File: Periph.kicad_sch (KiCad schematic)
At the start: 9 parts, among them U10 W25Q128JVSS, U8 ICM-42688-P

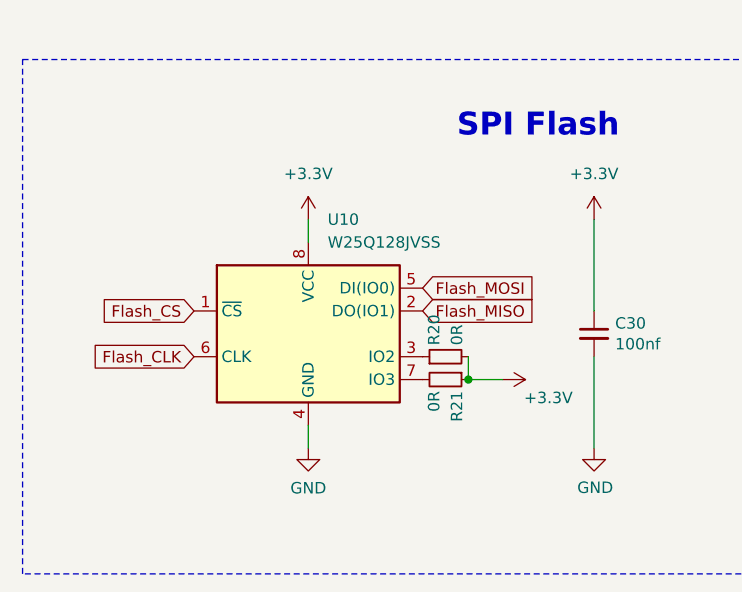
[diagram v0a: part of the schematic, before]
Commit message: update spi flash and ws2812b
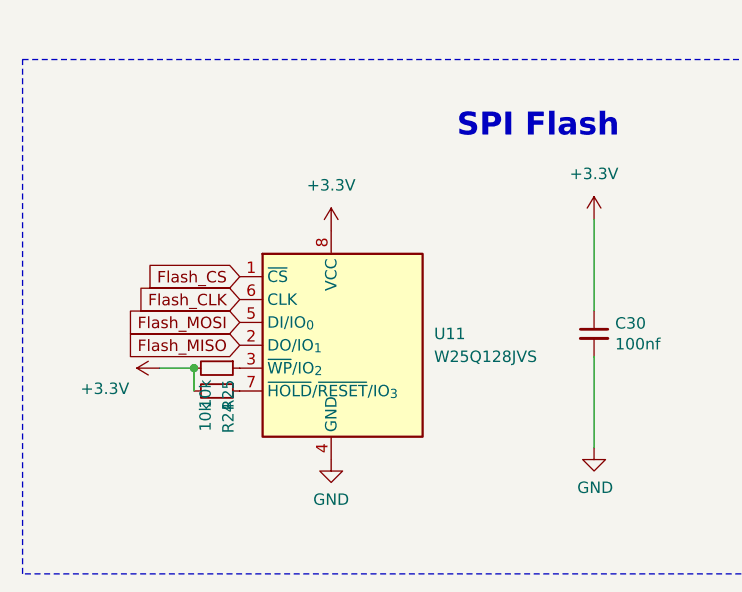
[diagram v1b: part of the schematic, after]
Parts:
- removed R20, R21: 0R, Resistor_SMD:R_0402_1005Metric, symbol Device:R_Small
- removed U10: W25Q128JVSS, Package_SO:SOIC-8_5.23x5.23mm_P1.27mm, symbol Memory_Flash:W25Q32JVSS
- added R24, R25: 10k, Resistor_SMD:R_0402_1005Metric, symbol Device:R_Small
- added U11: W25Q128JVS, Package_SO:SOIC-8_5.3x5.3mm_P1.27mm, symbol Memory_Flash:W25Q128JVS
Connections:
- net +3.3V: now also R24.2, R25.2, U11.8 (VCC)
- net Flash_CLK: now also U11.6 (CLK)
- net Flash_CS: now also U11.1 (~{CS})
- net Flash_MISO: now also U11.2 (DO/IO_{1})
- net Flash_MOSI: now also U11.5 (DI/IO_{0})
- net GND: now also U11.4 (GND)
- new net: R25.1, U11.3 (~{WP}/IO_{2})
- new net: R24.1, U11.7 (~{HOLD}/~{RESET}/IO_{3})

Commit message: update library
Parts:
- C24: renamed from C23; value 0.1u -> C_Small
- C25: renamed from C24; value 2u2 -> C_Small
- C26: renamed from C25; value 10n -> C_Small
- C27: renamed from C30; value 100nf -> C_Small
- R12: renamed from R19; value 10k -> R_Small
- R13: renamed from R25; value 10k -> R_Small
- R14: renamed from R24; value 10k -> R_Small
- U8: footprint mylib:PQFN50P300X250X97-14N -> ICM-42688-P:PQFN50P300X250X97-14N
- renumbered U11 to U9
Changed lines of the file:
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@@
 		(on_board yes)
 		(dnp no)
-		(property "Reference" "R25"
+		(property "Reference" "R13"
 			(at 67.31 151.13 0)
 			(effects
@@
 			)
 		)
-		(property "Value" "10k"
+		(property "Value" "R_Small"
 			(at 64.77 151.13 0)
 			(effects
@@
 			(project "MX_IMU"
 				(path "/8ed38441-7d4e-4e89-870f-07e11c6dce38/57f4b5bf-da86-4b65-9b05-7c9ef99c472c"
-					(reference "R25")
+					(reference "R13")
 					(unit 1)
 				)
@@
 		(on_board yes)
 		(dnp no)
-		(property "Reference" "#PWR078"
+		(property "Reference" "#PWR067"
 			(at 63.5 149.86 0)
 			(effects
@@
 			(project "MX_IMU"
 				(path "/8ed38441-7d4e-4e89-870f-07e11c6dce38/57f4b5bf-da86-4b65-9b05-7c9ef99c472c"
-					(reference "#PWR078")
+					(reference "#PWR067")
 					(unit 1)
 				)
@@
 		(dnp no)
 		(fields_autoplaced yes)
-		(property "Reference" "#PWR060"
+		(property "Reference" "#PWR061"
 			(at 143.51 64.77 0)
 			(effects
@@
 			(project "MX_IMU"
 				(path "/8ed38441-7d4e-4e89-870f-07e11c6dce38/57f4b5bf-da86-4b65-9b05-7c9ef99c472c"
-					(reference "#PWR060")
+					(reference "#PWR061")
 					(unit 1)
 				)
@@
 		(dnp no)
 		(fields_autoplaced yes)
-		(property "Reference" "#PWR075"
+		(property "Reference" "#PWR064"
 			(at 107.95 137.16 0)
 			(effects
@@
 			(project ""
 				(path "/8ed38441-7d4e-4e89-870f-07e11c6dce38/57f4b5bf-da86-4b65-9b05-7c9ef99c472c"
-					(reference "#PWR075")
+					(reference "#PWR064")
 					(unit 1)
 				)
@@
 		(dnp no)
 		(fields_autoplaced yes)
-		(property "Reference" "#PWR062"
+		(property "Reference" "#PWR063"
 			(at 113.03 102.87 0)
 			(effects
@@
 			(project "MX_IMU"
 				(path "/8ed38441-7d4e-4e89-870f-07e11c6dce38/57f4b5bf-da86-4b65-9b05-7c9ef99c472c"
-					(reference "#PWR062")
+					(reference "#PWR063")
 					(unit 1)
 				)
@@
 		(on_board yes)
 		(dnp no)
-		(property "Reference" "C30"
+		(property "Reference" "C27"
 			(at 110.2868 144.8816 0)
 			(effects
@@
 			)
 		)
-		(property "Value" "100nf"
+		(property "Value" "C_Small"
 			(at 110.2868 147.193 0)
 			(effects
@@
 			(project "MX_IMU"
 				(path "/8ed38441-7d4e-4e89-870f-07e11c6dce38/57f4b5bf-da86-4b65-9b05-7c9ef99c472c"
-					(reference "C30")
+					(reference "C27")
 					(unit 1)
 				)
@@
 		(on_board yes)
 		(dnp no)
-		(property "Reference" "#PWR0104"
+		(property "Reference" "#PWR068"
 			(at 107.95 165.1 0)
 			(effects
@@
 			(project "MX_IMU"
 				(path "/8ed38441-7d4e-4e89-870f-07e11c6dce38/57f4b5bf-da86-4b65-9b05-7c9ef99c472c"
-					(reference "#PWR0104")
+					(reference "#PWR068")
 					(unit 1)
 				)
@@
 		(on_board yes)
 		(dnp no)
-		(property "Reference" "C24"
+		(property "Reference" "C25"
 			(at 156.21 66.04 0)
 			(effects
@@
 			)
 		)
-		(property "Value" "2u2"
+		(property "Value" "C_Small"
 			(at 156.21 68.58 0)
 			(effects
@@
 			(project "MX_IMU"
 				(path "/8ed38441-7d4e-4e89-870f-07e11c6dce38/57f4b5bf-da86-4b65-9b05-7c9ef99c472c"
-					(reference "C24")
+					(reference "C25")
 					(unit 1)
 				)
@@
 		(dnp no)
 		(fields_autoplaced yes)
-		(property "Reference" "C23"
+		(property "Reference" "C24"
 			(at 146.05 66.0462 0)
 			(effects
@@
 			)
 		)
-		(property "Value" "0.1u"
+		(property "Value" "C_Small"
 			(at 146.05 68.5862 0)
 			(effects
@@
 			(project "MX_IMU"
 				(path "/8ed38441-7d4e-4e89-870f-07e11c6dce38/57f4b5bf-da86-4b65-9b05-7c9ef99c472c"
-					(reference "C23")
+					(reference "C24")
 					(unit 1)
 				)
@@
 		(on_board yes)
 		(dnp no)
-		(property "Reference" "R19"
+		(property "Reference" "R12"
 			(at 135.89 142.24 0)
 			(effects
@@
 			)
 		)
-		(property "Value" "10k"
+		(property "Value" "R_Small"
 			(at 135.89 144.78 0)
 			(effects
@@
 			(project "MX_IMU"
 				(path "/8ed38441-7d4e-4e89-870f-07e11c6dce38/57f4b5bf-da86-4b65-9b05-7c9ef99c472c"
-					(reference "R19")
+					(reference "R12")
 					(unit 1)
 				)
@@
 		(dnp no)
 		(fields_autoplaced yes)
-		(property "Reference" "#PWR061"
+		(property "Reference" "#PWR062"
 			(at 162.56 80.01 0)
 			(effects
@@
 			(project "MX_IMU"
 				(path "/8ed38441-7d4e-4e89-870f-07e11c6dce38/57f4b5bf-da86-4b65-9b05-7c9ef99c472c"
-					(reference "#PWR061")
+					(reference "#PWR062")
 					(unit 1)
 				)
@@
 		(dnp no)
 		(fields_autoplaced yes)
-		(property "Reference" "#PWR079"
+		(property "Reference" "#PWR069"
 			(at 78.74 166.37 0)
 			(effects
@@
 			(project "MX_IMU"
 				(path "/8ed38441-7d4e-4e89-870f-07e11c6dce38/57f4b5bf-da86-4b65-9b05-7c9ef99c472c"
-					(reference "#PWR079")
+					(reference "#PWR069")
 					(unit 1)
 				)
@@
 		(dnp no)
 		(fields_autoplaced yes)
-		(property "Reference" "#PWR076"
+		(property "Reference" "#PWR066"
 			(at 134.62 142.24 0)
 			(effects
@@
 			(project ""
 				(path "/8ed38441-7d4e-4e89-870f-07e11c6dce38/57f4b5bf-da86-4b65-9b05-7c9ef99c472c"
-					(reference "#PWR076")
+					(reference "#PWR066")
 					(unit 1)
 				)
@@
 		(on_board yes)
 		(dnp no)
-		(property "Reference" "R24"
+		(property "Reference" "R14"
 			(at 67.31 153.67 0)
 			(effects
@@
 			)
 		)
-		(property "Value" "10k"
+		(property "Value" "R_Small"
 			(at 64.77 153.67 0)
 			(effects
@@
 			(project "MX_IMU"
 				(path "/8ed38441-7d4e-4e89-870f-07e11c6dce38/57f4b5bf-da86-4b65-9b05-7c9ef99c472c"
-					(reference "R24")
+					(reference "R14")
 					(unit 1)
 				)
@@
 		(dnp no)
 		(fields_autoplaced yes)
-		(property "Reference" "#PWR059"
+		(property "Reference" "#PWR060"
 			(at 114.3 64.77 0)
 			(effects
@@
 			(project "MX_IMU"
 				(path "/8ed38441-7d4e-4e89-870f-07e11c6dce38/57f4b5bf-da86-4b65-9b05-7c9ef99c472c"
-					(reference "#PWR059")
+					(reference "#PWR060")
 					(unit 1)
 				)
@@
 			)
 		)
-		(property "Footprint" "mylib:PQFN50P300X250X97-14N"
+		(property "Footprint" "ICM-42688-P:PQFN50P300X250X97-14N"
 			(at 85.09 78.74 0)
 			(effects
@@
 		(dnp no)
 		(fields_autoplaced yes)
-		(property "Reference" "U11"
+		(property "Reference" "U9"
 			(at 90.17 146.0499 0)
 			(effects
@@
 			(project ""
 				(path "/8ed38441-7d4e-4e89-870f-07e11c6dce38/57f4b5bf-da86-4b65-9b05-7c9ef99c472c"
-					(reference "U11")
+					(reference "U9")
 					(unit 1)
 				)
@@
 		(dnp no)
 		(fields_autoplaced yes)
-		(property "Reference" "C25"
+		(property "Reference" "C26"
 			(at 165.1 66.0462 0)
 			(effects
@@
 			)
 		)
-		(property "Value" "10n"
+		(property "Value" "C_Small"
 			(at 165.1 68.5862 0)
 			(effects
@@
 			(project "MX_IMU"
 				(path "/8ed38441-7d4e-4e89-870f-07e11c6dce38/57f4b5bf-da86-4b65-9b05-7c9ef99c472c"
-					(reference "C25")
+					(reference "C26")
 					(unit 1)
 				)
@@
 		(dnp no)
 		(fields_autoplaced yes)
-		(property "Reference" "#PWR073"
+		(property "Reference" "#PWR065"
 			(at 78.74 138.43 0)
 			(effects
@@
 			(project "MX_IMU"
 				(path "/8ed38441-7d4e-4e89-870f-07e11c6dce38/57f4b5bf-da86-4b65-9b05-7c9ef99c472c"
-					(reference "#PWR073")
-					(unit 1)
-				)
+					(reference "#PWR065")
+					(unit 1)
+				)

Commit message: clean files
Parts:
- U8: footprint ICM-42688-P:PQFN50P300X250X97-14N -> mylib:ICM42688p
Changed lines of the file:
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@@
 			)
 		)
-		(property "Footprint" "ICM-42688-P:PQFN50P300X250X97-14N"
+		(property "Footprint" "mylib:ICM42688p"
 			(at 85.09 78.74 0)
 			(effects

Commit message: update
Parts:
- renumbered C27 to C24, C24 to C25, C25 to C26, C26 to C27, R13 to R12, R14 to R13, R12 to R14, U9 to U8, U8 to U9
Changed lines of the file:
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@@
 		(on_board yes)
 		(dnp no)
-		(property "Reference" "R13"
+		(property "Reference" "R12"
 			(at 67.31 151.13 0)
 			(effects
@@
 			(project "MX_IMU"
 				(path "/8ed38441-7d4e-4e89-870f-07e11c6dce38/57f4b5bf-da86-4b65-9b05-7c9ef99c472c"
-					(reference "R13")
+					(reference "R12")
 					(unit 1)
 				)
@@
 		(on_board yes)
 		(dnp no)
-		(property "Reference" "#PWR067"
+		(property "Reference" "#PWR060"
 			(at 63.5 149.86 0)
 			(effects
@@
 			(project "MX_IMU"
 				(path "/8ed38441-7d4e-4e89-870f-07e11c6dce38/57f4b5bf-da86-4b65-9b05-7c9ef99c472c"
-					(reference "#PWR067")
+					(reference "#PWR060")
 					(unit 1)
 				)
@@
 		(dnp no)
 		(fields_autoplaced yes)
-		(property "Reference" "#PWR061"
+		(property "Reference" "#PWR068"
 			(at 143.51 64.77 0)
 			(effects
@@
 			(project "MX_IMU"
 				(path "/8ed38441-7d4e-4e89-870f-07e11c6dce38/57f4b5bf-da86-4b65-9b05-7c9ef99c472c"
-					(reference "#PWR061")
+					(reference "#PWR068")
 					(unit 1)
 				)
@@
 		(dnp no)
 		(fields_autoplaced yes)
-		(property "Reference" "#PWR064"
+		(property "Reference" "#PWR063"
 			(at 107.95 137.16 0)
 			(effects
@@
 			(project ""
 				(path "/8ed38441-7d4e-4e89-870f-07e11c6dce38/57f4b5bf-da86-4b65-9b05-7c9ef99c472c"
-					(reference "#PWR064")
+					(reference "#PWR063")
 					(unit 1)
 				)
@@
 		(dnp no)
 		(fields_autoplaced yes)
-		(property "Reference" "#PWR063"
+		(property "Reference" "#PWR065"
 			(at 113.03 102.87 0)
 			(effects
@@
 			(project "MX_IMU"
 				(path "/8ed38441-7d4e-4e89-870f-07e11c6dce38/57f4b5bf-da86-4b65-9b05-7c9ef99c472c"
-					(reference "#PWR063")
+					(reference "#PWR065")
 					(unit 1)
 				)
@@
 		(on_board yes)
 		(dnp no)
-		(property "Reference" "C27"
+		(property "Reference" "C24"
 			(at 110.2868 144.8816 0)
 			(effects
@@
 			(project "MX_IMU"
 				(path "/8ed38441-7d4e-4e89-870f-07e11c6dce38/57f4b5bf-da86-4b65-9b05-7c9ef99c472c"
-					(reference "C27")
+					(reference "C24")
 					(unit 1)
 				)
@@
 		(on_board yes)
 		(dnp no)
-		(property "Reference" "#PWR068"
+		(property "Reference" "#PWR064"
 			(at 107.95 165.1 0)
 			(effects
@@
 			(project "MX_IMU"
 				(path "/8ed38441-7d4e-4e89-870f-07e11c6dce38/57f4b5bf-da86-4b65-9b05-7c9ef99c472c"
-					(reference "#PWR068")
+					(reference "#PWR064")
 					(unit 1)
 				)
@@
 		(on_board yes)
 		(dnp no)
-		(property "Reference" "C25"
+		(property "Reference" "C26"
 			(at 156.21 66.04 0)
 			(effects
@@
 			(project "MX_IMU"
 				(path "/8ed38441-7d4e-4e89-870f-07e11c6dce38/57f4b5bf-da86-4b65-9b05-7c9ef99c472c"
-					(reference "C25")
+					(reference "C26")
 					(unit 1)
 				)
@@
 		(dnp no)
 		(fields_autoplaced yes)
-		(property "Reference" "C24"
+		(property "Reference" "C25"
 			(at 146.05 66.0462 0)
 			(effects
@@
 			(project "MX_IMU"
 				(path "/8ed38441-7d4e-4e89-870f-07e11c6dce38/57f4b5bf-da86-4b65-9b05-7c9ef99c472c"
-					(reference "C24")
+					(reference "C25")
 					(unit 1)
 				)
@@
 		(on_board yes)
 		(dnp no)
-		(property "Reference" "R12"
+		(property "Reference" "R14"
 			(at 135.89 142.24 0)
 			(effects
@@
 			(project "MX_IMU"
 				(path "/8ed38441-7d4e-4e89-870f-07e11c6dce38/57f4b5bf-da86-4b65-9b05-7c9ef99c472c"
-					(reference "R12")
+					(reference "R14")
 					(unit 1)
 				)
@@
 		(dnp no)
 		(fields_autoplaced yes)
-		(property "Reference" "#PWR062"
+		(property "Reference" "#PWR069"
 			(at 162.56 80.01 0)
 			(effects
@@
 			(project "MX_IMU"
 				(path "/8ed38441-7d4e-4e89-870f-07e11c6dce38/57f4b5bf-da86-4b65-9b05-7c9ef99c472c"
-					(reference "#PWR062")
+					(reference "#PWR069")
 					(unit 1)
 				)
@@
 		(dnp no)
 		(fields_autoplaced yes)
-		(property "Reference" "#PWR069"
+		(property "Reference" "#PWR062"
 			(at 78.74 166.37 0)
 			(effects
@@
 			(project "MX_IMU"
 				(path "/8ed38441-7d4e-4e89-870f-07e11c6dce38/57f4b5bf-da86-4b65-9b05-7c9ef99c472c"
-					(reference "#PWR069")
+					(reference "#PWR062")
 					(unit 1)
 				)
@@
 		(dnp no)
 		(fields_autoplaced yes)
-		(property "Reference" "#PWR066"
+		(property "Reference" "#PWR067"
 			(at 134.62 142.24 0)
 			(effects
@@
 			(project ""
 				(path "/8ed38441-7d4e-4e89-870f-07e11c6dce38/57f4b5bf-da86-4b65-9b05-7c9ef99c472c"
-					(reference "#PWR066")
+					(reference "#PWR067")
 					(unit 1)
 				)
@@
 		(on_board yes)
 		(dnp no)
-		(property "Reference" "R14"
+		(property "Reference" "R13"
 			(at 67.31 153.67 0)
 			(effects
@@
 			(project "MX_IMU"
 				(path "/8ed38441-7d4e-4e89-870f-07e11c6dce38/57f4b5bf-da86-4b65-9b05-7c9ef99c472c"
-					(reference "R14")
+					(reference "R13")
 					(unit 1)
 				)
@@
 		(dnp no)
 		(fields_autoplaced yes)
-		(property "Reference" "#PWR060"
+		(property "Reference" "#PWR066"
 			(at 114.3 64.77 0)
 			(effects
@@
 			(project "MX_IMU"
 				(path "/8ed38441-7d4e-4e89-870f-07e11c6dce38/57f4b5bf-da86-4b65-9b05-7c9ef99c472c"
-					(reference "#PWR060")
+					(reference "#PWR066")
 					(unit 1)
 				)
@@
 		(dnp no)
 		(fields_autoplaced yes)
-		(property "Reference" "U8"
+		(property "Reference" "U9"
 			(at 85.09 58.166 0)
 			(effects
@@
 			(project "MX_IMU"
 				(path "/8ed38441-7d4e-4e89-870f-07e11c6dce38/57f4b5bf-da86-4b65-9b05-7c9ef99c472c"
-					(reference "U8")
+					(reference "U9")
 					(unit 1)
 				)
@@
 		(dnp no)
 		(fields_autoplaced yes)
-		(property "Reference" "U9"
+		(property "Reference" "U8"
 			(at 90.17 146.0499 0)
 			(effects
@@
 			(project ""
 				(path "/8ed38441-7d4e-4e89-870f-07e11c6dce38/57f4b5bf-da86-4b65-9b05-7c9ef99c472c"
-					(reference "U9")
+					(reference "U8")
 					(unit 1)
 				)
@@
 		(dnp no)
 		(fields_autoplaced yes)
-		(property "Reference" "C26"
+		(property "Reference" "C27"
 			(at 165.1 66.0462 0)
 			(effects
@@
 			(project "MX_IMU"
 				(path "/8ed38441-7d4e-4e89-870f-07e11c6dce38/57f4b5bf-da86-4b65-9b05-7c9ef99c472c"
-					(reference "C26")
+					(reference "C27")
 					(unit 1)
 				)
@@
 		(dnp no)
 		(fields_autoplaced yes)
-		(property "Reference" "#PWR065"
+		(property "Reference" "#PWR061"
 			(at 78.74 138.43 0)
 			(effects
@@
 			(project "MX_IMU"
 				(path "/8ed38441-7d4e-4e89-870f-07e11c6dce38/57f4b5bf-da86-4b65-9b05-7c9ef99c472c"
-					(reference "#PWR065")
-					(unit 1)
-				)
+					(reference "#PWR061")
+					(unit 1)
+				)
